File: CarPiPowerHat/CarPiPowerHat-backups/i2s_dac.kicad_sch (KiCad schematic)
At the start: 23 parts, among them J8 AudioJack2_Ground, Q4 DMG2305, U7 AP2112-3.3K, U8 UDA1334ATS

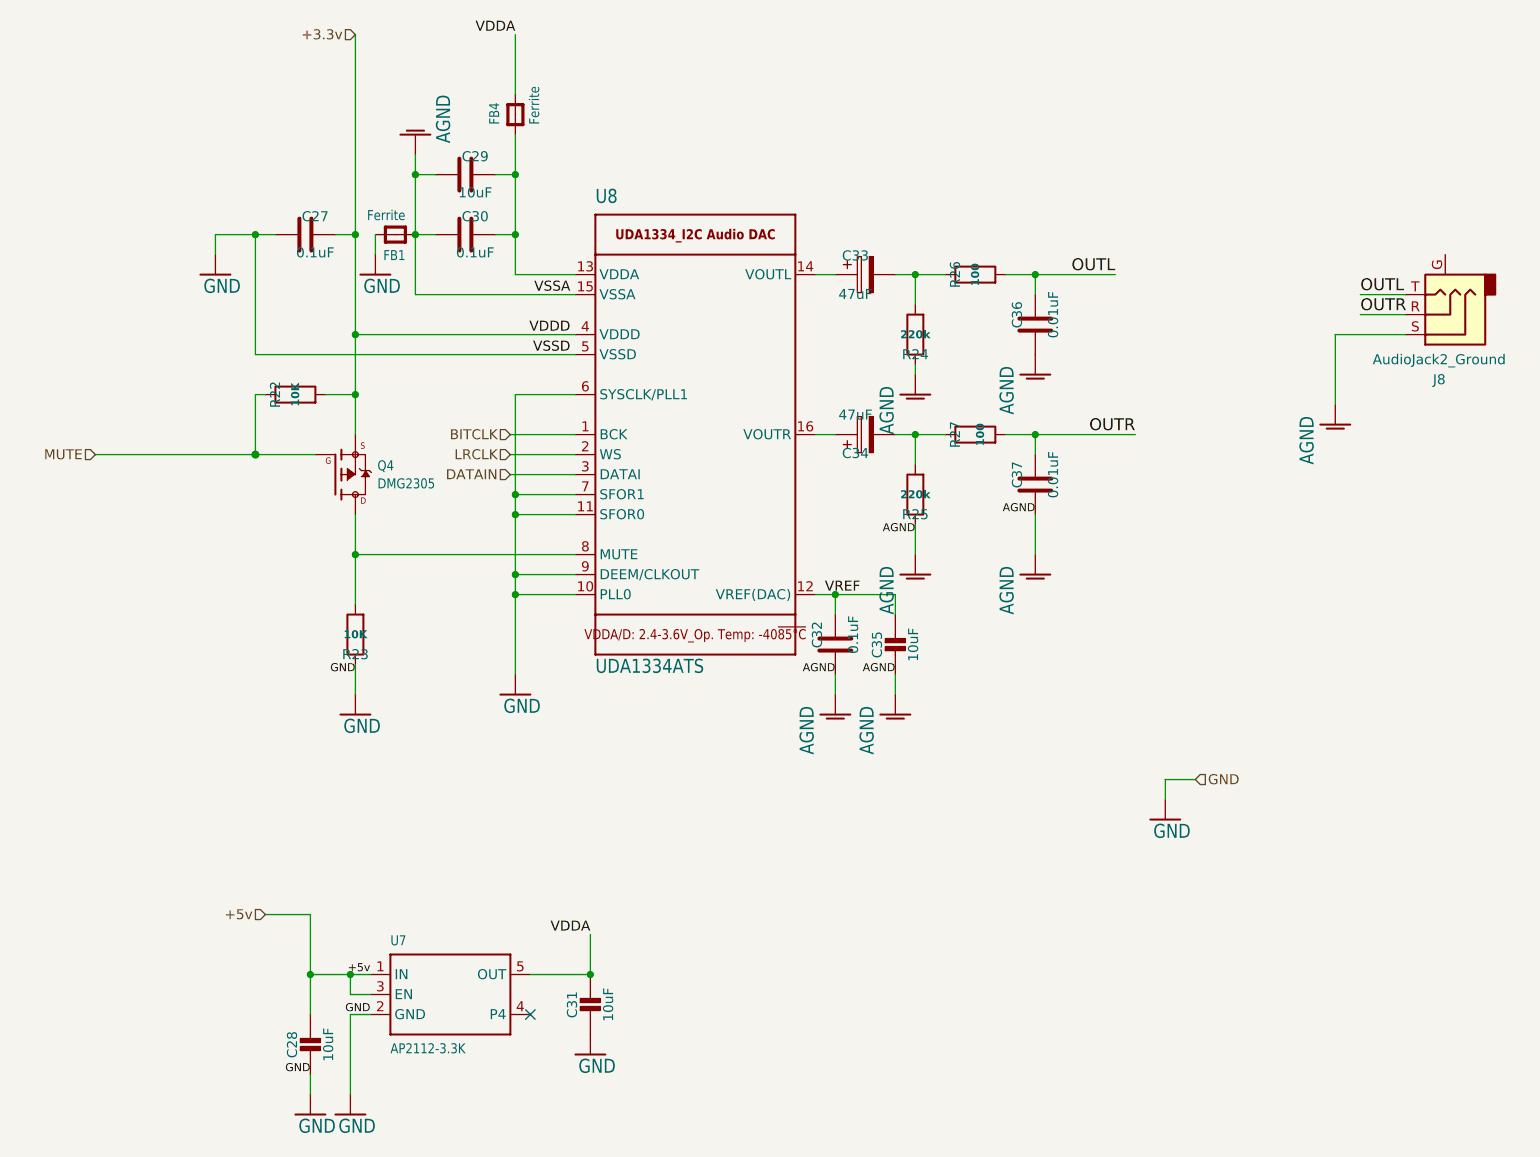
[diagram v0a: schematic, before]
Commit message: Repositioning of connectors
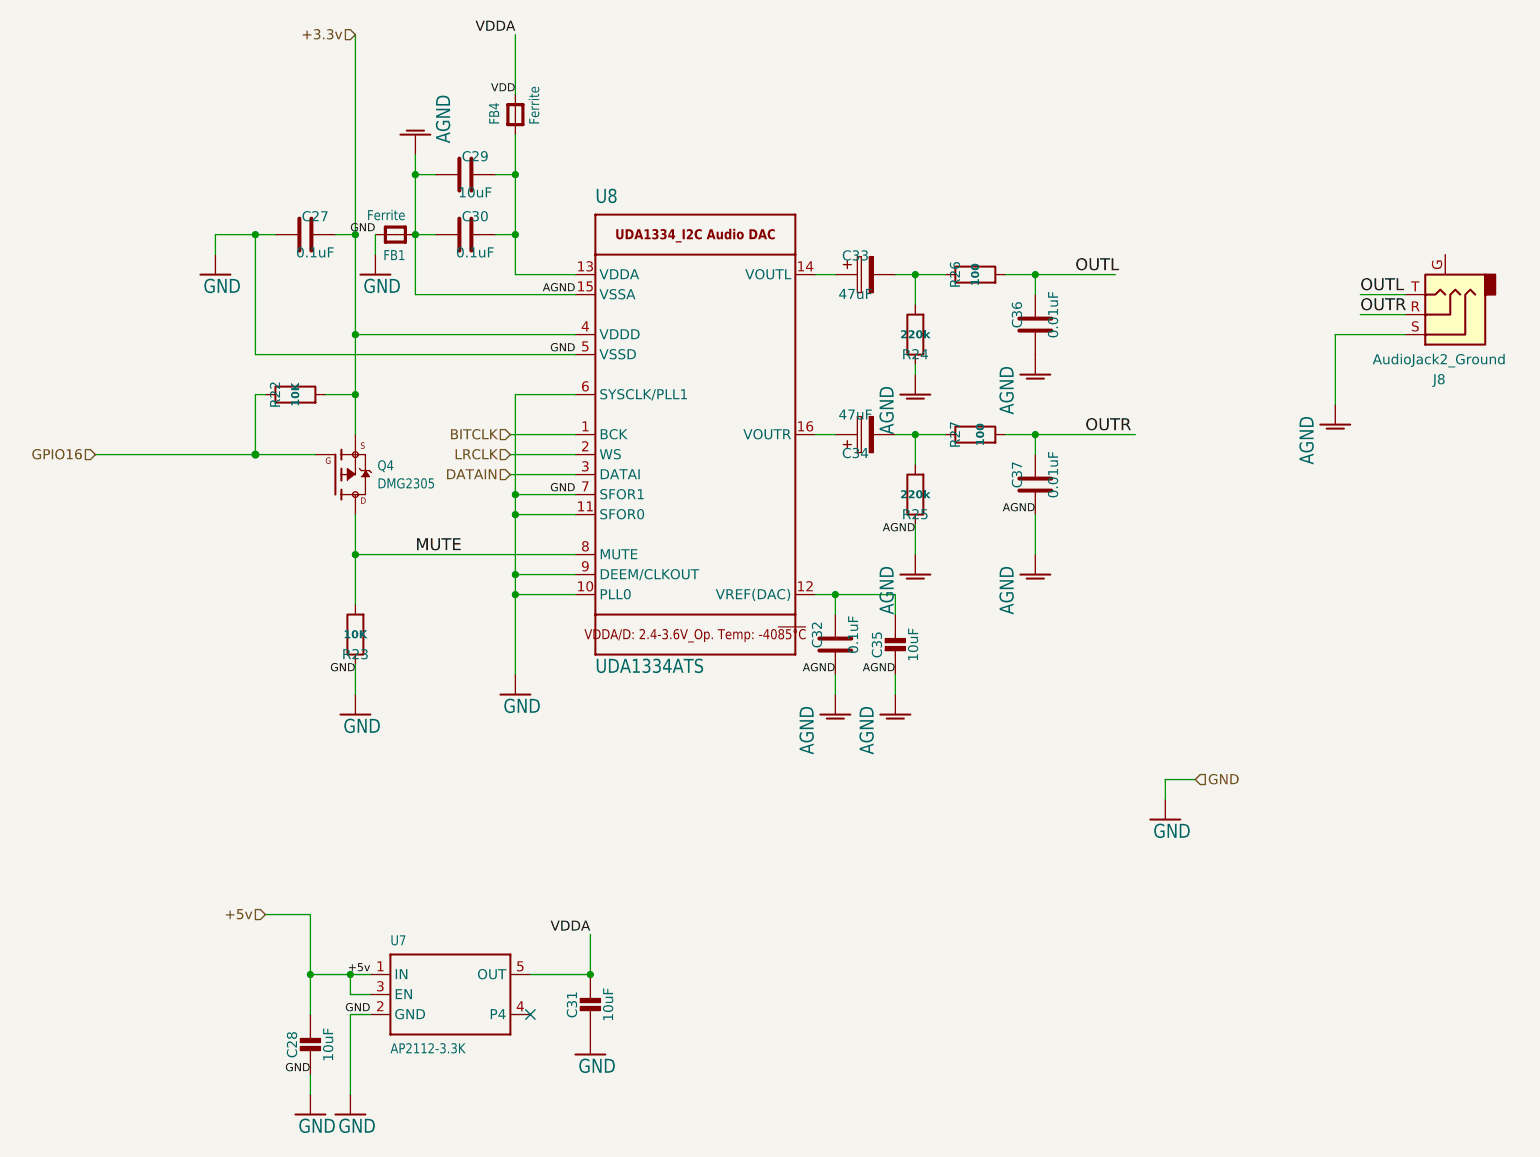
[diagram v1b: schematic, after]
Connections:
- net MUTE: now also Q4.3 (D), R23.2, U8.8 (MUTE); no longer Q4.1 (G), R22.1
- net VDDA renamed VDD
- net VREF: no longer names the net of C32.1, C35.1, U8.12 (VREF(DAC))
- new net GPIO16: Q4.1 (G), R22.1
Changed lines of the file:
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@@
     (effects (font (size 1.016 1.016)) (justify right bottom))
+  )
+  (label "GND" (at 66.675 58.42 180)
+    (effects (font (size 1.016 1.016)) (justify right bottom))
+  )
+  (label "MUTE" (at 71.755 99.06 0)
+    (effects (font (size 1.5113 1.5113)) (justify left bottom))
   )
   (label "VDDA" (at 84.455 33.02 180)
     (effects (font (size 1.27 1.27)) (justify right bottom))
   )
-  (label "VSSA" (at 91.44 66.04 180)
-    (effects (font (size 1.27 1.27)) (justify right bottom))
+  (label "VDD" (at 84.455 40.64 180)
+    (effects (font (size 1.016 1.016)) (justify right bottom))
   )
-  (label "VDDD" (at 91.44 71.12 180)
-    (effects (font (size 1.27 1.27)) (justify right bottom))
+  (label "AGND" (at 92.075 66.04 180)
+    (effects (font (size 1.016 1.016)) (justify right bottom))
   )
-  (label "VSSD" (at 91.44 73.66 180)
-    (effects (font (size 1.27 1.27)) (justify right bottom))
+  (label "GND" (at 92.075 73.66 180)
+    (effects (font (size 1.016 1.016)) (justify right bottom))
+  )
+  (label "GND" (at 92.075 91.44 180)
+    (effects (font (size 1.016 1.016)) (justify right bottom))
   )
   (label "VDDA" (at 93.98 147.32 180)
@@
   (label "AGND" (at 125.095 114.3 180)
     (effects (font (size 1.016 1.016)) (justify right bottom))
-  )
-  (label "VREF" (at 128.27 104.14 180)
-    (effects (font (size 1.27 1.27)) (justify right bottom))
   )
   (label "AGND" (at 132.715 114.3 180)
@@
     (effects (font (size 1.016 1.016)) (justify right bottom))
   )
-  (label "OUTL" (at 160.655 63.5 180)
-    (effects (font (size 1.5113 1.5113)) (justify right bottom))
+  (label "OUTL" (at 155.575 63.5 0)
+    (effects (font (size 1.5113 1.5113)) (justify left bottom))
   )
-  (label "OUTR" (at 163.195 83.82 180)
-    (effects (font (size 1.5113 1.5113)) (justify right bottom))
+  (label "OUTR" (at 156.845 83.82 0)
+    (effects (font (size 1.5113 1.5113)) (justify left bottom))
   )
   (label "OUTL" (at 191.77 66.04 0)
@@
     (effects (font (size 1.5113 1.5113)) (justify left bottom))
   )
-  (hierarchical_label "MUTE" (shape input) (at 31.115 86.36 180)
+  (hierarchical_label "GPIO16" (shape input) (at 31.115 86.36 180)
     (effects (font (size 1.27 1.27)) (justify right))
   )
